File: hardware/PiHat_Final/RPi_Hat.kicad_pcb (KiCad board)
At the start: 2 copper layers, 65 x 56.5 mm, 78 parts, among them J1 SMACONN, J2 RPi_GPIO, P1 USB_OTG, P2 BATT, P3 THERM, Q1 AFT05MS003N, SW1 PWR_VOL, U1 MCP3021, U2 MCP73833, U3 TPS61027, U4 Si4464, U5 MMG3H21NT1, U6 SKY13374, Y1 30MHz

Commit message: Worked on RF Layout.
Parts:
- removed R10, R11: R, Resistors_SMD:R_0603
- C22, C26, C27, L10, L11, U1: moved to B.Cu
- moved RV1 96.6 mm to (155.2, 96.9)
- moved U6 80.0 mm to (127.7, 117.5)
- moved C18 77.3 mm to (158.8, 121.2), turned to 0 degrees
- moved C9 73.2 mm to (158.5, 114.4), turned to 180 degrees
- moved L9 67.6 mm to (144.1, 113.9), turned to 180 degrees
- moved L11 64.7 mm to (138.3, 118.8), turned to 270 degrees
- moved C10 62.0 mm to (162.4, 113.3), turned to 270 degrees
- moved L10 61.9 mm to (141.1, 113.7), turned to 270 degrees
- moved L4 61.5 mm to (167.6, 114.3), turned to 180 degrees
- moved C21 58.4 mm to (148.5, 118.2), turned to 0 degrees
- moved C30 58.3 mm to (137.0, 116.3), turned to 0 degrees
- moved C25 55.6 mm to (142.2, 119.2), turned to 0 degrees
- moved C24 53.4 mm to (144.3, 111.5), turned to 0 degrees
- moved C26 53.2 mm to (138.3, 113.4), turned to 90 degrees
- moved C22 52.2 mm to (143.7, 113.3), turned to 270 degrees
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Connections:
- U6 pad 11: TX_PWR -> RXI
- U6 pad 5: RXI -> TX_PWR
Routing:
- net RXI: track 0.00 -> 38.8 mm
- net +3V3: track 0.00 -> 17.4 mm
- net Net-(C9-Pad1): track 0.00 -> 16.9 mm
- net Net-(C14-Pad2): track 0.00 -> 15.6 mm
- net Net-(C10-Pad2): track 0.00 -> 14.1 mm
- net Net-(C27-Pad1): track 0.00 -> 11.9 mm, vias 0 -> 1
- net 5VU: track 57.1 -> 68.4 mm
- net TX_PWR: track 0.00 -> 10.8 mm
- net Net-(C15-Pad2): track 0.00 -> 10.3 mm
- net VOL: track 0.00 -> 8.91 mm
- net Net-(L8-Pad2): track 0.00 -> 8.11 mm
- net Net-(C11-Pad1): track 0.00 -> 7.52 mm
- net VBAT: track 49.2 -> 56.4 mm, vias 0 -> 2
- net (no net): track 6.96 -> 0.00 mm
- net Net-(C19-Pad2): track 0.00 -> 6.96 mm
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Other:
- board size 65 x 56.5 mm -> 65 x 56 mm

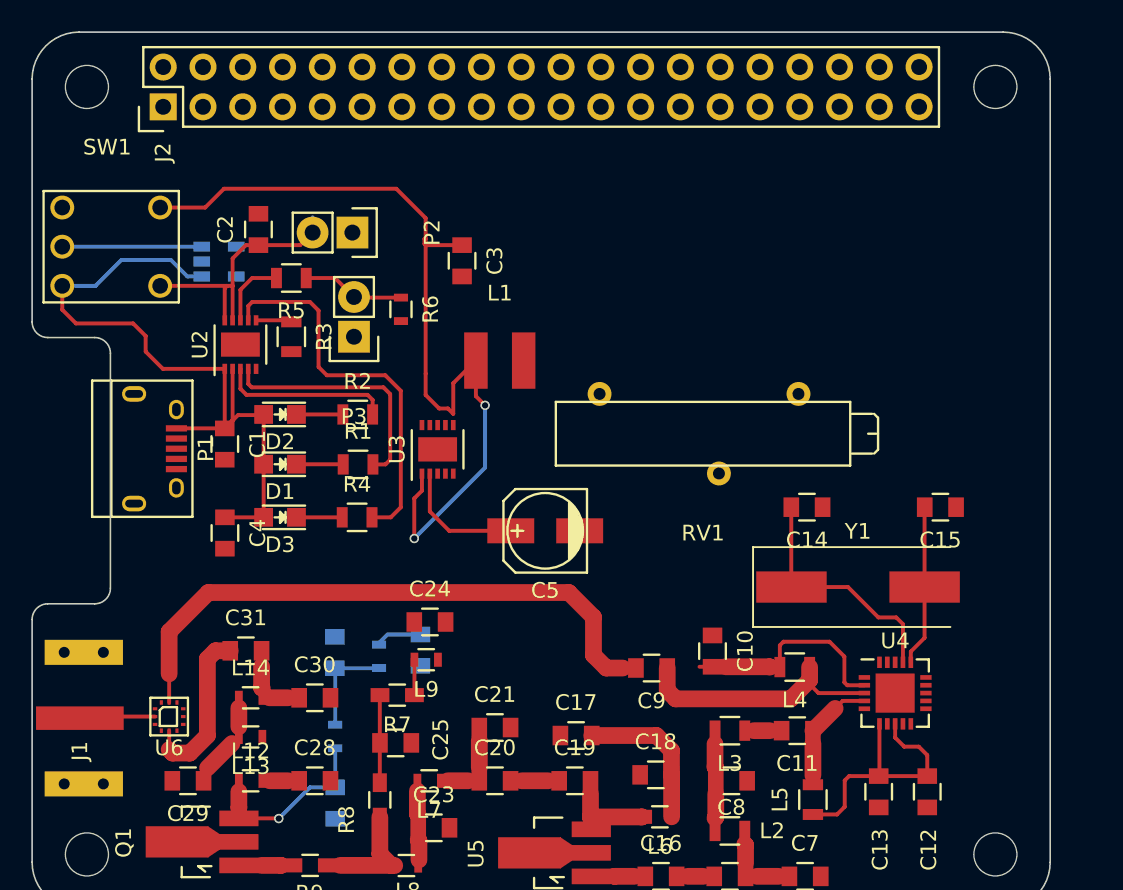
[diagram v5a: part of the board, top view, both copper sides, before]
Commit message: Transciever wiring & Power Distribution Changes, modified footprint for Edge SMA, swapped TX/RX on ANTSEL
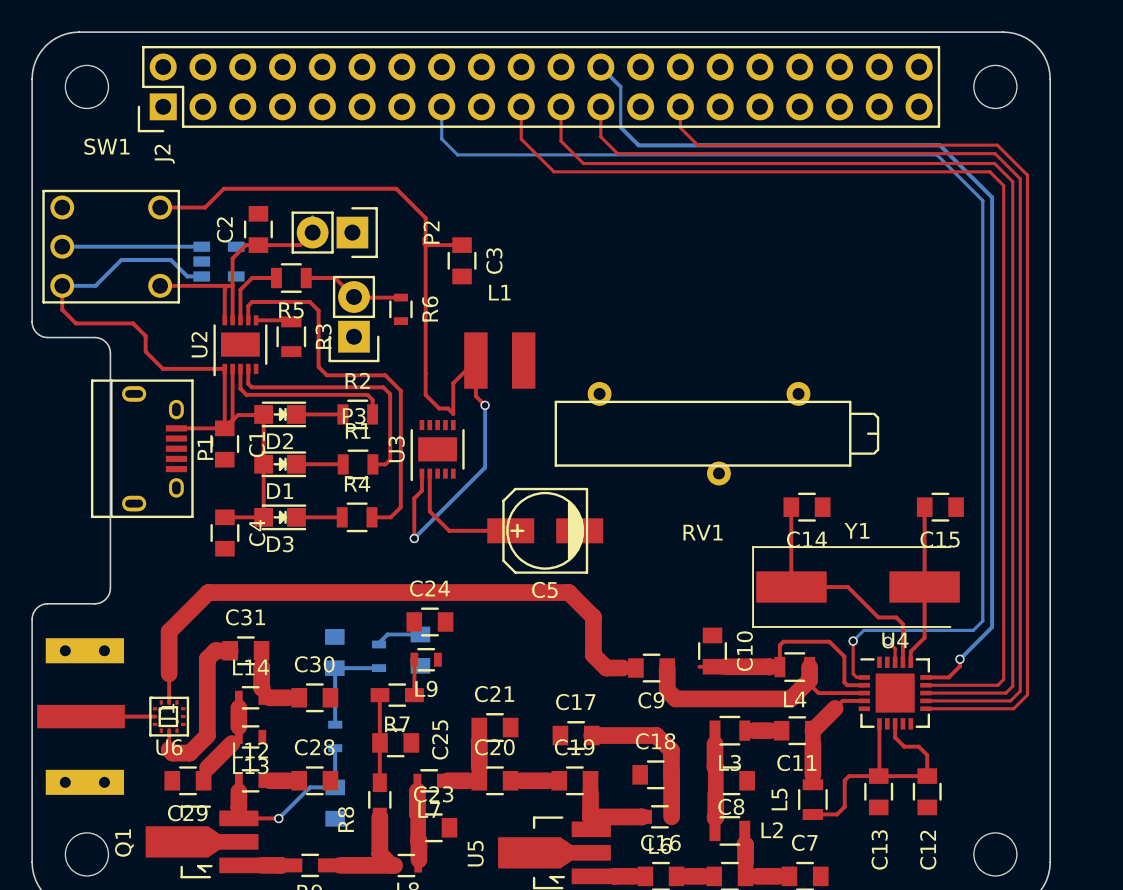
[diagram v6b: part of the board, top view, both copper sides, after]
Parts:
- moved J1 0.12 mm to (122.1, 117.5)
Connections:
- J2 pad 1: Net-(J2-Pad1) -> +3V3
- J2 pad 10: Net-(J2-Pad10) -> (no net)
- J2 pad 11: Net-(J2-Pad11) -> (no net)
- J2 pad 12: Net-(J2-Pad12) -> (no net)
- J2 pad 13: Net-(J2-Pad13) -> (no net)
- J2 pad 14: Net-(J2-Pad14) -> GND
- J2 pad 15: Net-(J2-Pad15) -> SHDN
- J2 pad 16: Net-(J2-Pad16) -> (no net)
- J2 pad 17: Net-(J2-Pad17) -> +3V3
- J2 pad 18: Net-(J2-Pad18) -> (no net)
- J2 pad 19: Net-(J2-Pad19) -> MOSI
- J2 pad 2: Net-(J2-Pad2) -> 5VU
- J2 pad 20: Net-(J2-Pad20) -> GND
- J2 pad 21: Net-(J2-Pad21) -> MISO
- J2 pad 22: Net-(J2-Pad22) -> (no net)
- J2 pad 23: Net-(J2-Pad23) -> SCLK
- J2 pad 24: Net-(J2-Pad24) -> nSEL
- J2 pad 25: Net-(J2-Pad25) -> GND
- J2 pad 26: Net-(J2-Pad26) -> (no net)
- J2 pad 27: Net-(J2-Pad27) -> nIRQ
- J2 pad 28: Net-(J2-Pad28) -> (no net)
- J2 pad 29: Net-(J2-Pad29) -> (no net)
- J2 pad 3: Net-(J2-Pad3) -> (no net)
- J2 pad 30: Net-(J2-Pad30) -> GND
- J2 pad 31: Net-(J2-Pad31) -> (no net)
- J2 pad 32: Net-(J2-Pad32) -> (no net)
- J2 pad 33: Net-(J2-Pad33) -> (no net)
- J2 pad 34: Net-(J2-Pad34) -> (no net)
- J2 pad 35: Net-(J2-Pad35) -> (no net)
- J2 pad 36: Net-(J2-Pad36) -> (no net)
- J2 pad 37: Net-(J2-Pad37) -> (no net)
- J2 pad 38: Net-(J2-Pad38) -> (no net)
- J2 pad 39: Net-(J2-Pad39) -> GND
- J2 pad 4: Net-(J2-Pad4) -> 5VU
- J2 pad 40: Net-(J2-Pad40) -> (no net)
- J2 pad 5: Net-(J2-Pad5) -> (no net)
- J2 pad 6: Net-(J2-Pad6) -> GND
- J2 pad 7: Net-(J2-Pad7) -> (no net)
- J2 pad 8: Net-(J2-Pad8) -> (no net)
- J2 pad 9: Net-(J2-Pad9) -> GND
- P1 pad 2: Net-(P1-Pad2) -> (no net)
- P1 pad 3: Net-(P1-Pad3) -> (no net)
- P1 pad 4: Net-(P1-Pad4) -> (no net)
- U1 pad 4: SDA -> (no net)
- U1 pad 5: SCL -> (no net)
- U3 pad 3: Net-(U3-Pad3) -> (no net)
- U3 pad 4: Net-(U3-Pad4) -> (no net)
- U3 pad 7: Net-(U3-Pad7) -> (no net)
- U4 pad 10: Net-(U4-Pad10) -> (no net)
- U4 pad 13: SDO -> MISO
- U4 pad 14: SDI -> MOSI
- U4 pad 19: Net-(U4-Pad19) -> (no net)
- U4 pad 20: Net-(U4-Pad20) -> (no net)
- U4 pad 5: Net-(U4-Pad5) -> (no net)
- U4 pad 7: Net-(U4-Pad7) -> (no net)
- U4 pad 9: Net-(U4-Pad9) -> (no net)
- U6 pad 1: Net-(U6-Pad1) -> (no net)
- U6 pad 7: SEL_1 -> (no net)
- U6 pad 8: SEL_2 -> (no net)
- U6 pad 9: SEL_1 -> +3V3
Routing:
- net SHDN: track 0.00 -> 76.8 mm, vias 0 -> 1
- net MOSI: track 0.00 -> 70.7 mm
- net MISO: track 0.00 -> 70.0 mm
- net SCLK: track 0.00 -> 68.8 mm
- net nIRQ: track 0.00 -> 64.8 mm
- net nSEL: track 0.00 -> 63.2 mm, vias 0 -> 1
- net GND: track 0.00 -> 1.54 mm, vias 0 -> 1

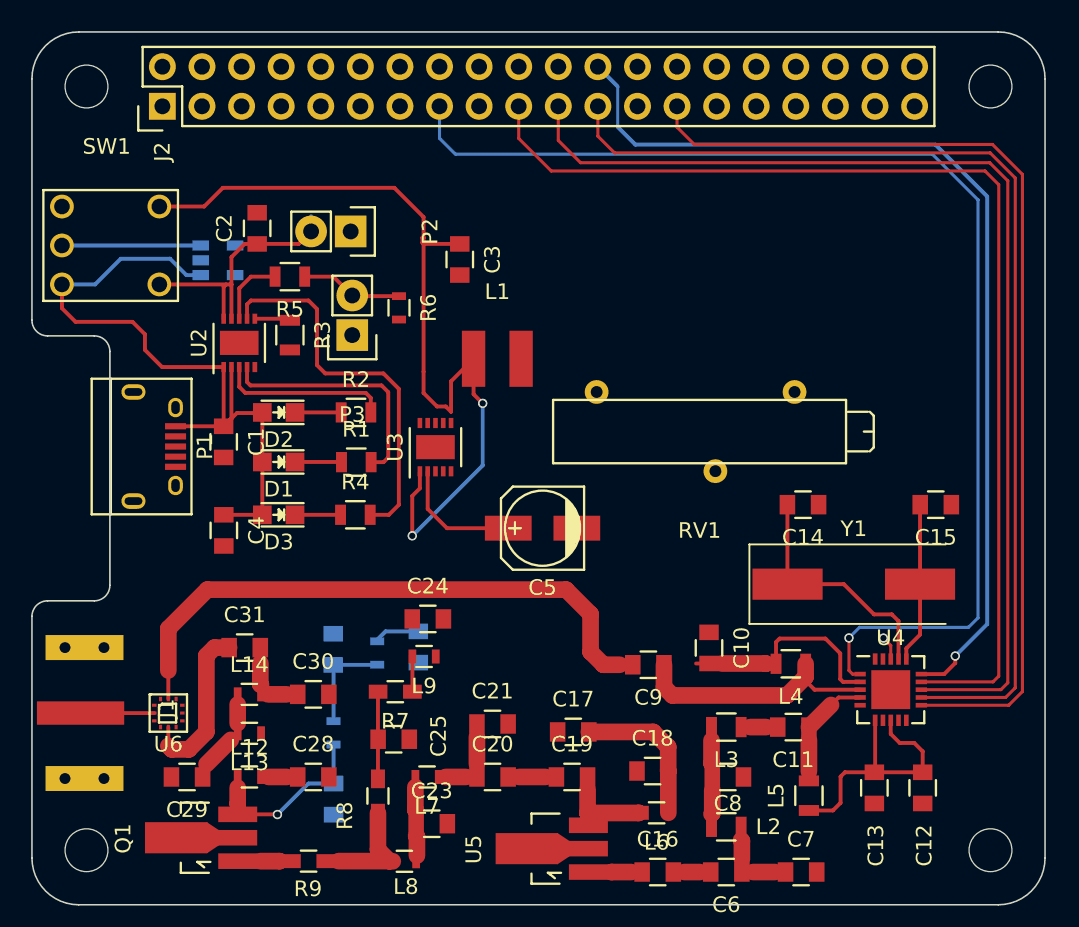
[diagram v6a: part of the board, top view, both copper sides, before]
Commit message: Reworked some power wiring, pausing to explore options regarding power routing.
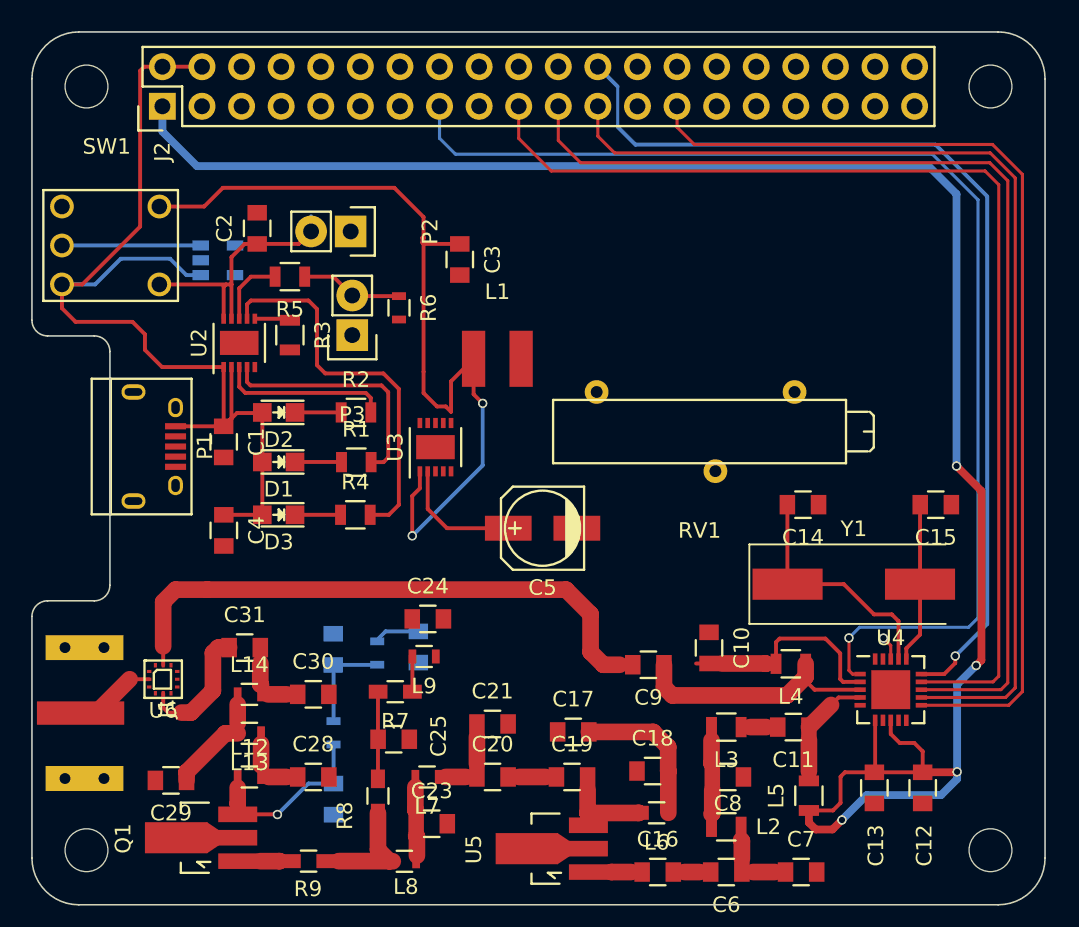
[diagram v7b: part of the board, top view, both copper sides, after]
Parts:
- moved U6 2.19 mm to (127.4, 115.3)
- moved C29 1.05 mm to (127.9, 121.8)
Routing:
- net +3V3: track 17.4 -> 124.5 mm, vias 0 -> 4
- net 5VU: track 68.4 -> 89.0 mm
- net Net-(C28-Pad1): track 2.35 -> 5.16 mm
- net TX_PWR: track 10.8 -> 8.43 mm
- net Net-(J1-Pad1): track 4.84 -> 6.10 mm
- net Net-(C29-Pad1): track 6.24 -> 7.36 mm
- net RXI: track 38.8 -> 38.0 mm
